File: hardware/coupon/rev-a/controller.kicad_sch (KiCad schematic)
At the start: 21 parts, among them SW1 EVQP7J01P, U3 ESP32-S3-WROOM-1U-N16R8

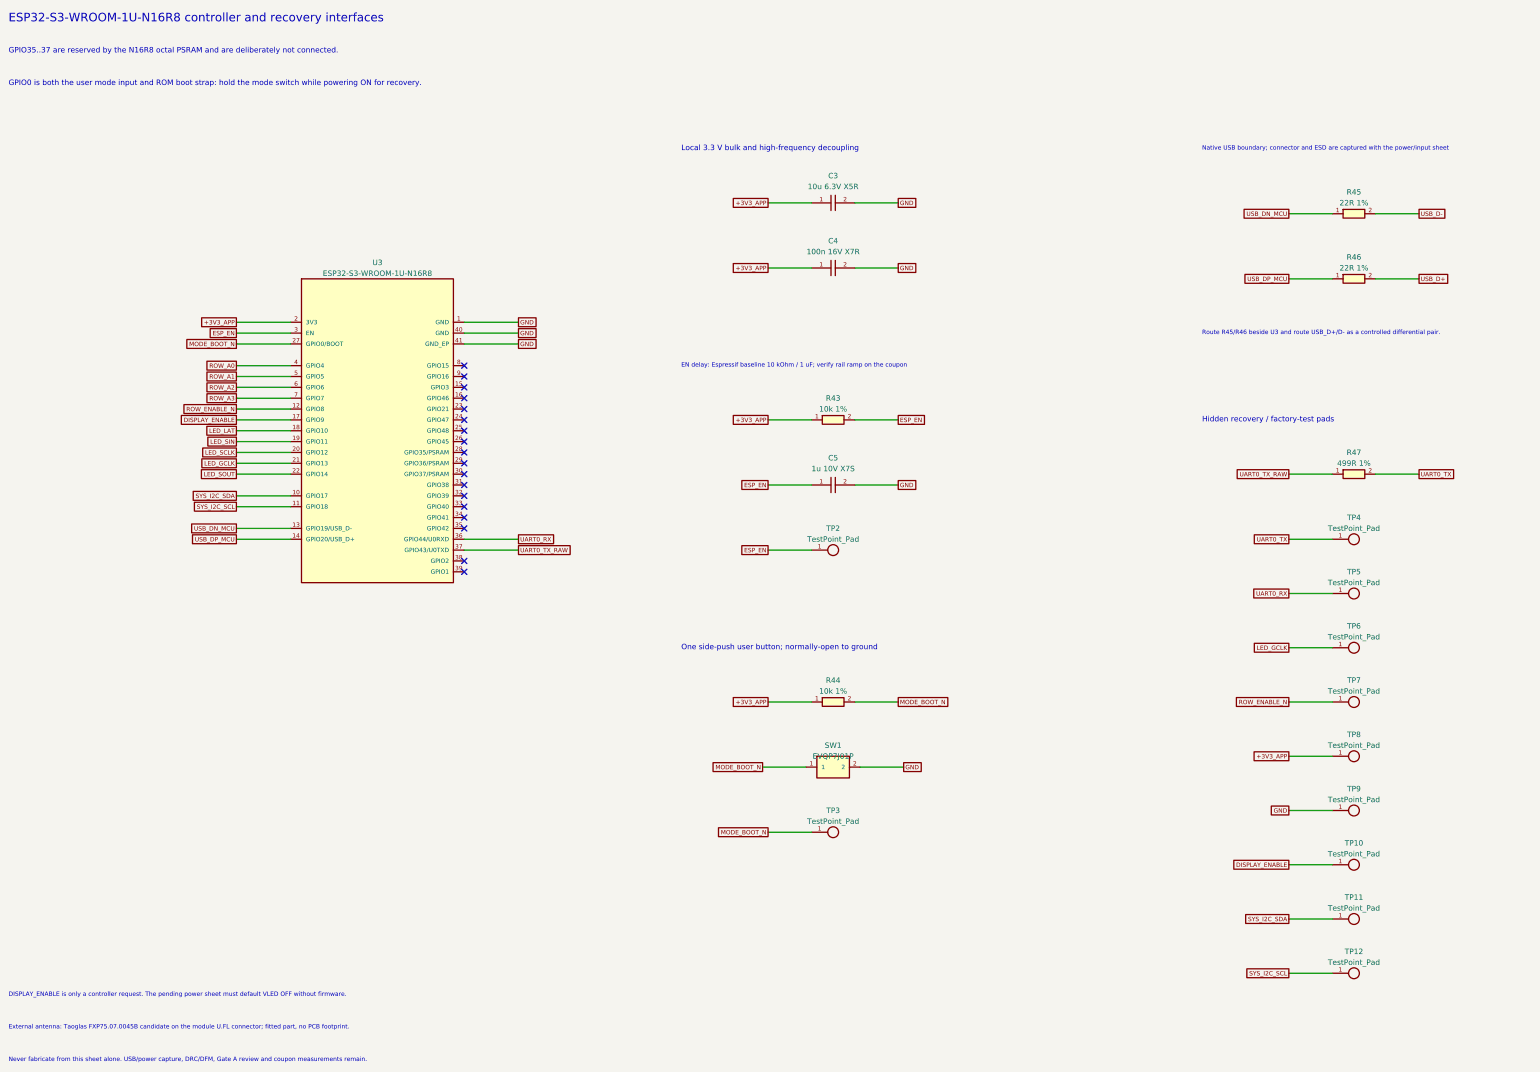
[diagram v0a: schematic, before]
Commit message: Capture USB detection and switched data path after native logic review
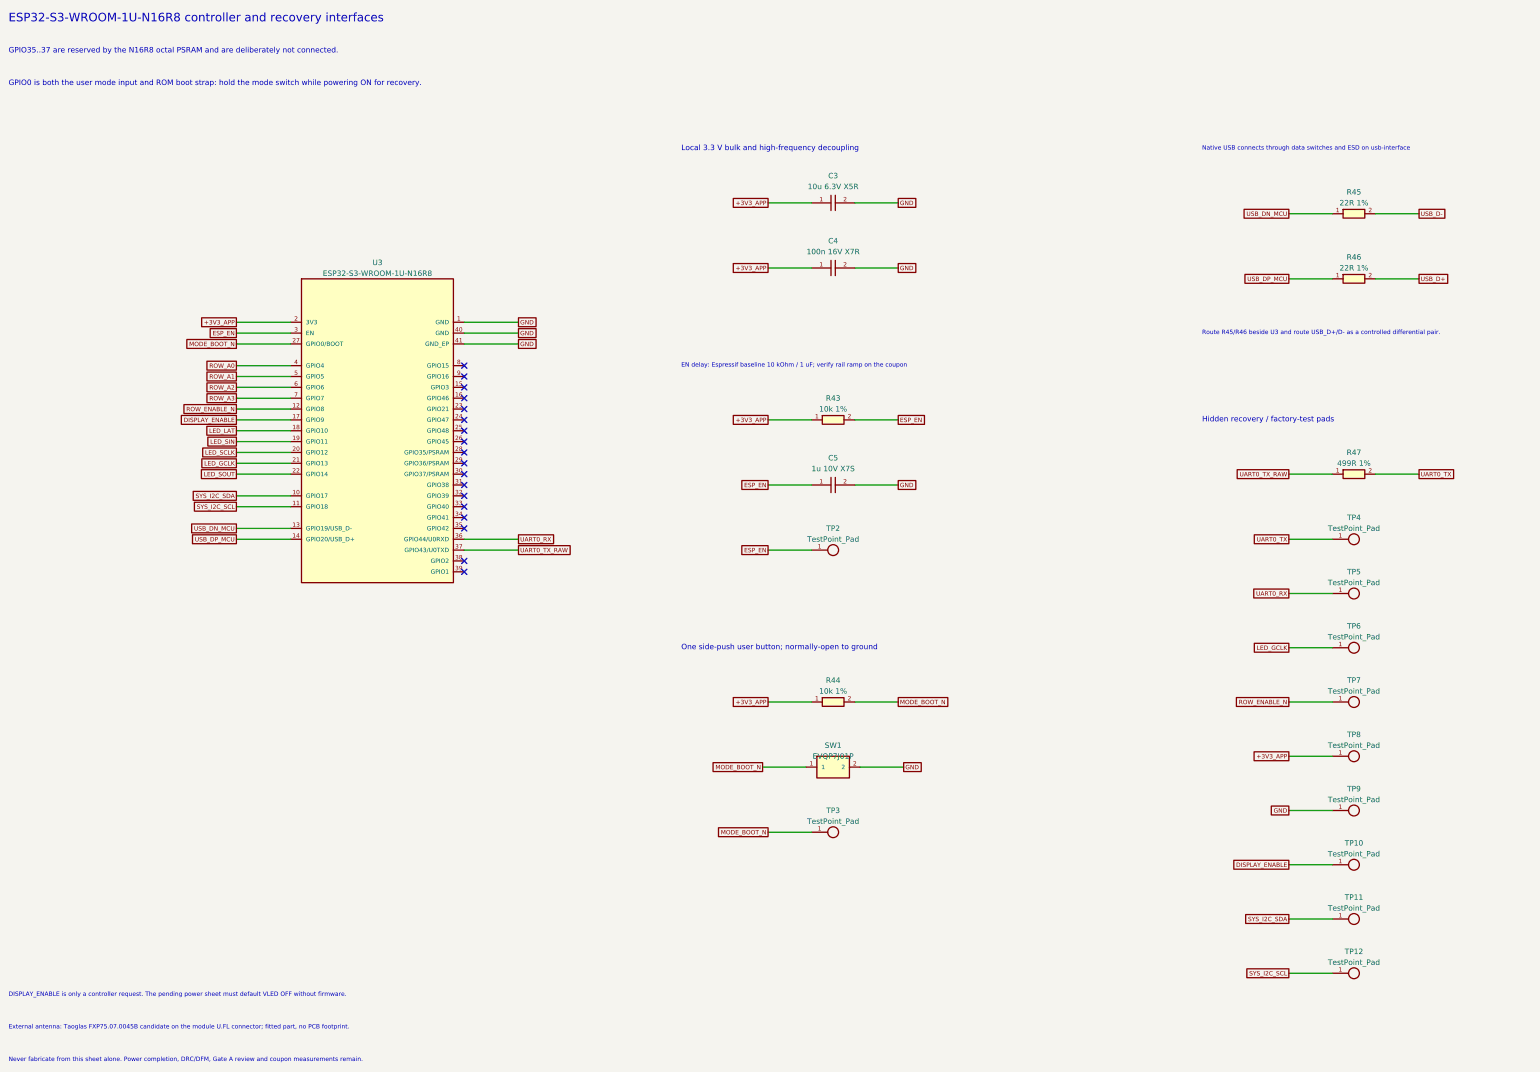
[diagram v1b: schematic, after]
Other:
- note added: "Native USB connects through data switches and ESD on usb-interface"
- note added: "Never fabricate from this sheet alone. Power completion, DRC/DFM, Gate A review and coupon measurements remain."
- note removed: "Native USB boundary; connector and ESD are captured with the power/input sheet"
- note removed: "Never fabricate from this sheet alone. USB/power capture, DRC/DFM, Gate A review and coupon measurements remain."
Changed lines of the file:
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@@
 (generator_version "1.0")
 (paper "A2")
-(title_block (title "Coupon Rev A - ESP32-S3 controller") (rev "A-draft") (comment 1 "SPDX-License-Identifier: CERN-OHL-S-2.0") (comment 2 "USB connector/ESD and switched rail sources remain on the pending power sheet"))
+(title_block (title "Coupon Rev A - ESP32-S3 controller") (rev "A-draft") (comment 1 "SPDX-License-Identifier: CERN-OHL-S-2.0") (comment 2 "USB data connects to usb-interface; switched rail sources remain pending"))
 (text "ESP32-S3-WROOM-1U-N16R8 controller and recovery interfaces" (at 20.32 20.32 0) (effects (font (size 2.0 2.0)) (justify left)))
 (text "GPIO35..37 are reserved by the N16R8 octal PSRAM and are deliberately not connected." (at 20.32 27.94 0) (effects (font (size 1.27 1.27)) (justify left)))
@@
 (wire (pts (xy 208.280 210.820) (xy 198.120 210.820)) (stroke (width 0) (type default)))
 (global_label "MODE_BOOT_N" (shape passive) (at 198.120 210.820 180) (effects (font (size 1.016 1.016)) (justify right)) (property "Intersheetrefs" "${INTERSHEET_REFS}" (at 198.120 210.820 0) (effects (font (size 1.27 1.27)) (hide yes))))
-(text "Native USB boundary; connector and ESD are captured with the power/input sheet" (at 299.72 50.80 0) (effects (font (size 1.016 1.016)) (justify left)))
+(text "Native USB connects through data switches and ESD on usb-interface" (at 299.72 50.80 0) (effects (font (size 1.016 1.016)) (justify left)))
 (symbol (lib_id "rgb-badge-coupon:ERJ-2RKF22R0X") (at 335.280 66.040 0) (unit 1)
 (exclude_from_sim no) (in_bom yes) (on_board yes) (dnp no)
@@
 (text "DISPLAY_ENABLE is only a controller request. The pending power sheet must default VLED OFF without firmware." (at 20.32 248.92 0) (effects (font (size 1.016 1.016)) (justify left)))
 (text "External antenna: Taoglas FXP75.07.0045B candidate on the module U.FL connector; fitted part, no PCB footprint." (at 20.32 256.54 0) (effects (font (size 1.016 1.016)) (justify left)))
-(text "Never fabricate from this sheet alone. USB/power capture, DRC/DFM, Gate A review and coupon measurements remain." (at 20.32 264.16 0) (effects (font (size 1.016 1.016)) (justify left)))
+(text "Never fabricate from this sheet alone. Power completion, DRC/DFM, Gate A review and coupon measurements remain." (at 20.32 264.16 0) (effects (font (size 1.016 1.016)) (justify left)))
 (embedded_fonts no)
 )

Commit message: Normalize Panasonic ERJ order codes across coupon
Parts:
- R43, R44: symbol rgb-badge-coupon:ERJ-2RKF1002X -> rgb-badge-coupon:ERJ2RKF1002X; MPN ERJ-2RKF1002X -> ERJ2RKF1002X
- R45, R46: symbol rgb-badge-coupon:ERJ-2RKF22R0X -> rgb-badge-coupon:ERJ2RKF22R0X; MPN ERJ-2RKF22R0X -> ERJ2RKF22R0X
- R47: symbol rgb-badge-coupon:ERJ-2RKF4990X -> rgb-badge-coupon:ERJ2RKF4990X; MPN ERJ-2RKF4990X -> ERJ2RKF4990X
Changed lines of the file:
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@@
 (global_label "GND" (shape passive) (at 228.600 78.740 0) (effects (font (size 1.016 1.016)) (justify left)) (property "Intersheetrefs" "${INTERSHEET_REFS}" (at 228.600 78.740 0) (effects (font (size 1.27 1.27)) (hide yes))))
 (text "EN delay: Espressif baseline 10 kOhm / 1 uF; verify rail ramp on the coupon" (at 177.80 101.60 0) (effects (font (size 1.016 1.016)) (justify left)))
-(symbol (lib_id "rgb-badge-coupon:ERJ-2RKF1002X") (at 213.360 114.300 0) (unit 1)
+(symbol (lib_id "rgb-badge-coupon:ERJ2RKF1002X") (at 213.360 114.300 0) (unit 1)
 (exclude_from_sim no) (in_bom yes) (on_board yes) (dnp no)
 (property "Reference" "R43" (at 213.360 109.220 0) (effects (font (size 1.27 1.27))))
@@
 (property "Datasheet" "https://industrial.panasonic.com/cdbs/www-data/pdf/RDA0000/AOA0000C304.pdf" (at 213.360 114.300 0) (effects (font (size 1.27 1.27)) (hide yes)))
 (property "Manufacturer" "Panasonic" (at 213.360 114.300 0) (effects (font (size 1.27 1.27)) (hide yes)))
-(property "MPN" "ERJ-2RKF1002X" (at 213.360 114.300 0) (effects (font (size 1.27 1.27)) (hide yes)))
+(property "MPN" "ERJ2RKF1002X" (at 213.360 114.300 0) (effects (font (size 1.27 1.27)) (hide yes)))
 (pin "1")
 (pin "2")
@@
 (global_label "ESP_EN" (shape passive) (at 198.120 144.780 180) (effects (font (size 1.016 1.016)) (justify right)) (property "Intersheetrefs" "${INTERSHEET_REFS}" (at 198.120 144.780 0) (effects (font (size 1.27 1.27)) (hide yes))))
 (text "One side-push user button; normally-open to ground" (at 177.80 167.64 0) (effects (font (size 1.27 1.27)) (justify left)))
-(symbol (lib_id "rgb-badge-coupon:ERJ-2RKF1002X") (at 213.360 180.340 0) (unit 1)
+(symbol (lib_id "rgb-badge-coupon:ERJ2RKF1002X") (at 213.360 180.340 0) (unit 1)
 (exclude_from_sim no) (in_bom yes) (on_board yes) (dnp no)
 (property "Reference" "R44" (at 213.360 175.260 0) (effects (font (size 1.27 1.27))))
@@
 (property "Datasheet" "https://industrial.panasonic.com/cdbs/www-data/pdf/RDA0000/AOA0000C304.pdf" (at 213.360 180.340 0) (effects (font (size 1.27 1.27)) (hide yes)))
 (property "Manufacturer" "Panasonic" (at 213.360 180.340 0) (effects (font (size 1.27 1.27)) (hide yes)))
-(property "MPN" "ERJ-2RKF1002X" (at 213.360 180.340 0) (effects (font (size 1.27 1.27)) (hide yes)))
+(property "MPN" "ERJ2RKF1002X" (at 213.360 180.340 0) (effects (font (size 1.27 1.27)) (hide yes)))
 (pin "1")
 (pin "2")
@@
 (global_label "MODE_BOOT_N" (shape passive) (at 198.120 210.820 180) (effects (font (size 1.016 1.016)) (justify right)) (property "Intersheetrefs" "${INTERSHEET_REFS}" (at 198.120 210.820 0) (effects (font (size 1.27 1.27)) (hide yes))))
 (text "Native USB connects through data switches and ESD on usb-interface" (at 299.72 50.80 0) (effects (font (size 1.016 1.016)) (justify left)))
-(symbol (lib_id "rgb-badge-coupon:ERJ-2RKF22R0X") (at 335.280 66.040 0) (unit 1)
+(symbol (lib_id "rgb-badge-coupon:ERJ2RKF22R0X") (at 335.280 66.040 0) (unit 1)
 (exclude_from_sim no) (in_bom yes) (on_board yes) (dnp no)
 (property "Reference" "R45" (at 335.280 60.960 0) (effects (font (size 1.27 1.27))))
@@
 (property "Datasheet" "https://industrial.panasonic.com/cdbs/www-data/pdf/RDA0000/AOA0000C304.pdf" (at 335.280 66.040 0) (effects (font (size 1.27 1.27)) (hide yes)))
 (property "Manufacturer" "Panasonic" (at 335.280 66.040 0) (effects (font (size 1.27 1.27)) (hide yes)))
-(property "MPN" "ERJ-2RKF22R0X" (at 335.280 66.040 0) (effects (font (size 1.27 1.27)) (hide yes)))
+(property "MPN" "ERJ2RKF22R0X" (at 335.280 66.040 0) (effects (font (size 1.27 1.27)) (hide yes)))
 (pin "1")
 (pin "2")
@@
 (wire (pts (xy 340.360 66.040) (xy 350.520 66.040)) (stroke (width 0) (type default)))
 (global_label "USB_D-" (shape passive) (at 350.520 66.040 0) (effects (font (size 1.016 1.016)) (justify left)) (property "Intersheetrefs" "${INTERSHEET_REFS}" (at 350.520 66.040 0) (effects (font (size 1.27 1.27)) (hide yes))))
-(symbol (lib_id "rgb-badge-coupon:ERJ-2RKF22R0X") (at 335.280 81.280 0) (unit 1)
+(symbol (lib_id "rgb-badge-coupon:ERJ2RKF22R0X") (at 335.280 81.280 0) (unit 1)
 (exclude_from_sim no) (in_bom yes) (on_board yes) (dnp no)
 (property "Reference" "R46" (at 335.280 76.200 0) (effects (font (size 1.27 1.27))))
@@
 (property "Datasheet" "https://industrial.panasonic.com/cdbs/www-data/pdf/RDA0000/AOA0000C304.pdf" (at 335.280 81.280 0) (effects (font (size 1.27 1.27)) (hide yes)))
 (property "Manufacturer" "Panasonic" (at 335.280 81.280 0) (effects (font (size 1.27 1.27)) (hide yes)))
-(property "MPN" "ERJ-2RKF22R0X" (at 335.280 81.280 0) (effects (font (size 1.27 1.27)) (hide yes)))
+(property "MPN" "ERJ2RKF22R0X" (at 335.280 81.280 0) (effects (font (size 1.27 1.27)) (hide yes)))
 (pin "1")
 (pin "2")
@@
 (text "Route R45/R46 beside U3 and route USB_D+/D- as a controlled differential pair." (at 299.72 93.98 0) (effects (font (size 1.016 1.016)) (justify left)))
 (text "Hidden recovery / factory-test pads" (at 299.72 114.30 0) (effects (font (size 1.27 1.27)) (justify left)))
-(symbol (lib_id "rgb-badge-coupon:ERJ-2RKF4990X") (at 335.280 127.000 0) (unit 1)
+(symbol (lib_id "rgb-badge-coupon:ERJ2RKF4990X") (at 335.280 127.000 0) (unit 1)
 (exclude_from_sim no) (in_bom yes) (on_board yes) (dnp no)
 (property "Reference" "R47" (at 335.280 121.920 0) (effects (font (size 1.27 1.27))))
@@
 (property "Datasheet" "https://industrial.panasonic.com/cdbs/www-data/pdf/RDA0000/AOA0000C304.pdf" (at 335.280 127.000 0) (effects (font (size 1.27 1.27)) (hide yes)))
 (property "Manufacturer" "Panasonic" (at 335.280 127.000 0) (effects (font (size 1.27 1.27)) (hide yes)))
-(property "MPN" "ERJ-2RKF4990X" (at 335.280 127.000 0) (effects (font (size 1.27 1.27)) (hide yes)))
+(property "MPN" "ERJ2RKF4990X" (at 335.280 127.000 0) (effects (font (size 1.27 1.27)) (hide yes)))
 (pin "1")
 (pin "2")

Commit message: Separate controller row request from decoder enable
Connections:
- net ROW_ENABLE_N renamed ROW_ENABLE_REQ_N
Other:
- note added: "GPIO8 ROW_ENABLE_REQ_N is isolated from decoder E; DISPLAY_ENABLE is only a request. Hardware interlock pending."
- note removed: "DISPLAY_ENABLE is only a controller request. The pending power sheet must default VLED OFF without firmware."
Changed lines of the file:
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@@
 (global_label "SYS_I2C_SCL" (shape passive) (at 73.660 134.620 180) (effects (font (size 1.016 1.016)) (justify right)) (property "Intersheetrefs" "${INTERSHEET_REFS}" (at 73.660 134.620 0) (effects (font (size 1.27 1.27)) (hide yes))))
 (wire (pts (xy 86.360 111.760) (xy 73.660 111.760)) (stroke (width 0) (type default)))
-(global_label "ROW_ENABLE_N" (shape passive) (at 73.660 111.760 180) (effects (font (size 1.016 1.016)) (justify right)) (property "Intersheetrefs" "${INTERSHEET_REFS}" (at 73.660 111.760 0) (effects (font (size 1.27 1.27)) (hide yes))))
+(global_label "ROW_ENABLE_REQ_N" (shape passive) (at 73.660 111.760 180) (effects (font (size 1.016 1.016)) (justify right)) (property "Intersheetrefs" "${INTERSHEET_REFS}" (at 73.660 111.760 0) (effects (font (size 1.27 1.27)) (hide yes))))
 (wire (pts (xy 86.360 139.700) (xy 73.660 139.700)) (stroke (width 0) (type default)))
 (global_label "USB_DN_MCU" (shape passive) (at 73.660 139.700 180) (effects (font (size 1.016 1.016)) (justify right)) (property "Intersheetrefs" "${INTERSHEET_REFS}" (at 73.660 139.700 0) (effects (font (size 1.27 1.27)) (hide yes))))
@@
 (instances (project "rgb-badge-coupon" (path "/207fb68e-2ddb-46bb-8712-eba2f8c5eef6/c1aa0a05-857c-59e4-b6b1-f737e9508fa3" (reference "TP7") (unit 1)))))
 (wire (pts (xy 330.200 180.340) (xy 320.040 180.340)) (stroke (width 0) (type default)))
-(global_label "ROW_ENABLE_N" (shape passive) (at 320.040 180.340 180) (effects (font (size 1.016 1.016)) (justify right)) (property "Intersheetrefs" "${INTERSHEET_REFS}" (at 320.040 180.340 0) (effects (font (size 1.27 1.27)) (hide yes))))
+(global_label "ROW_ENABLE_REQ_N" (shape passive) (at 320.040 180.340 180) (effects (font (size 1.016 1.016)) (justify right)) (property "Intersheetrefs" "${INTERSHEET_REFS}" (at 320.040 180.340 0) (effects (font (size 1.27 1.27)) (hide yes))))
 (symbol (lib_id "rgb-badge-coupon:TestPoint_Pad") (at 335.280 193.040 0) (unit 1)
 (exclude_from_sim no) (in_bom no) (on_board yes) (dnp no)
@@
 (wire (pts (xy 330.200 243.840) (xy 320.040 243.840)) (stroke (width 0) (type default)))
 (global_label "SYS_I2C_SCL" (shape passive) (at 320.040 243.840 180) (effects (font (size 1.016 1.016)) (justify right)) (property "Intersheetrefs" "${INTERSHEET_REFS}" (at 320.040 243.840 0) (effects (font (size 1.27 1.27)) (hide yes))))
-(text "DISPLAY_ENABLE is only a controller request. The pending power sheet must default VLED OFF without firmware." (at 20.32 248.92 0) (effects (font (size 1.016 1.016)) (justify left)))
+(text "GPIO8 ROW_ENABLE_REQ_N is isolated from decoder E; DISPLAY_ENABLE is only a request. Hardware interlock pending." (at 20.32 248.92 0) (effects (font (size 1.016 1.016)) (justify left)))
 (text "External antenna: Taoglas FXP75.07.0045B candidate on the module U.FL connector; fitted part, no PCB footprint." (at 20.32 256.54 0) (effects (font (size 1.016 1.016)) (justify left)))
 (text "Never fabricate from this sheet alone. Power completion, DRC/DFM, Gate A review and coupon measurements remain." (at 20.32 264.16 0) (effects (font (size 1.016 1.016)) (justify left)))

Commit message: Capture output-isolated display interlock and screen complete fit
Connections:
- net DISPLAY_HEARTBEAT: now reaches U3.8 (GPIO15)
- net DISPLAY_ARM_CLK: now reaches U3.9 (GPIO16)
- no-connect marks 18 -> 16
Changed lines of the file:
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@@
 (wire (pts (xy 86.360 109.220) (xy 73.660 109.220)) (stroke (width 0) (type default)))
 (global_label "ROW_A3" (shape passive) (at 73.660 109.220 180) (effects (font (size 1.016 1.016)) (justify right)) (property "Intersheetrefs" "${INTERSHEET_REFS}" (at 73.660 109.220 0) (effects (font (size 1.27 1.27)) (hide yes))))
-(no_connect (at 127.000 101.600))
-(no_connect (at 127.000 104.140))
+(wire (pts (xy 127.000 101.600) (xy 139.700 101.600)) (stroke (width 0) (type default)))
+(global_label "DISPLAY_HEARTBEAT" (shape passive) (at 139.700 101.600 0) (effects (font (size 1.016 1.016)) (justify left)) (property "Intersheetrefs" "${INTERSHEET_REFS}" (at 139.700 101.600 0) (effects (font (size 1.27 1.27)) (hide yes))))
+(wire (pts (xy 127.000 104.140) (xy 139.700 104.140)) (stroke (width 0) (type default)))
+(global_label "DISPLAY_ARM_CLK" (shape passive) (at 139.700 104.140 0) (effects (font (size 1.016 1.016)) (justify left)) (property "Intersheetrefs" "${INTERSHEET_REFS}" (at 139.700 104.140 0) (effects (font (size 1.27 1.27)) (hide yes))))
 (wire (pts (xy 86.360 132.080) (xy 73.660 132.080)) (stroke (width 0) (type default)))
 (global_label "SYS_I2C_SDA" (shape passive) (at 73.660 132.080 180) (effects (font (size 1.016 1.016)) (justify right)) (property "Intersheetrefs" "${INTERSHEET_REFS}" (at 73.660 132.080 0) (effects (font (size 1.27 1.27)) (hide yes))))

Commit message: Correct all six exact Murata capacitor lands and preserve 59-edge routing
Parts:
- C3: footprint rgb-badge-coupon:C_Murata_GRM18_0603 -> rgb-badge-coupon:C_Murata_GRM188R60J106ME47_0603
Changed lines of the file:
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@@
 (property "Reference" "C3" (at 213.360 57.150 0) (effects (font (size 1.27 1.27))))
 (property "Value" "10u 6.3V X5R" (at 213.360 59.690 0) (effects (font (size 1.27 1.27))))
-(property "Footprint" "rgb-badge-coupon:C_Murata_GRM18_0603" (at 213.360 63.500 0) (effects (font (size 1.27 1.27)) (hide yes)))
+(property "Footprint" "rgb-badge-coupon:C_Murata_GRM188R60J106ME47_0603" (at 213.360 63.500 0) (effects (font (size 1.27 1.27)) (hide yes)))
 (property "Datasheet" "https://pim.murata.com/en-global/pim/details/?partNum=GRM188R60J106ME47D" (at 213.360 63.500 0) (effects (font (size 1.27 1.27)) (hide yes)))
 (property "Manufacturer" "Murata" (at 213.360 63.500 0) (effects (font (size 1.27 1.27)) (hide yes)))
